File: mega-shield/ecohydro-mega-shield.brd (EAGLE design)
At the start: 101.6 x 92.7 mm, 99 parts, among them IC1 MCP1700-330, IC2 DS1306E, IC3 74HC125D, IC4 AP3211KTR, Q1 IRLM5103, Q10 PBSS4021NT,215, Q11 PBSS4021NT,215, Q12 PBSS4021NT,215, Q13 PBSS4021NT,215, Q14 PBSS4021NT,215, Q15 PBSS4021NT,215, Q16 PBSS4021NT,215, Q17 IRLM5103, Q18 IRLM5103, Q19 IRLM5103, Q2 IRLM5103, Q20 PBSS4021NT,215, Q21 PBSS4021NT,215, Q22 PBSS4021NT,215, Q3 IRLM5103, Q4 IRLM5103, Q5 IRLM5103, Q6 IRLM5103, Q7 IRLM5103, Q8 IRLM5103, Q9 PBSS4021NT,215, U1 ARDUINO-MEGA

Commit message: Rev 1.1 with some fixes, not sent for production yet
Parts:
- removed A7: MKDS1/3-3,81, con-phoenix-381:3POL381
- added A15: MKDS1/3-3,81, con-phoenix-381:3POL381
- Q10, Q11, Q12, Q13, Q14, Q15, Q16, Q20, Q21, Q22, Q9: device semiconductors:SOT-23 -> semiconductors:SOT23
- R19: value 470R -> 1k; device passives:R0603-N -> passives:R0805
- moved A14 16.5 mm to (88.9, 4.45), turned to 0 degrees
- moved A12 14.0 mm to (61.0, 4.45)
- moved A9 14.0 mm to (19.1, 4.45)
- moved A8 14.0 mm to (5.08, 4.45)
- moved A10 14.0 mm to (33.0, 4.45)
- moved A11 14.0 mm to (47.0, 4.45)
- moved A13 14.0 mm to (74.9, 4.45)
- moved Q22 2.55 mm to (48.2, 71.0)
- moved Q20 1.58 mm to (12.3, 71.0)
- moved Q21 1.58 mm to (29.4, 71.0)
- moved Q17 1.00 mm to (51.8, 73.7)
- moved R20 1.00 mm to (51.8, 70.5)
- moved Q18 0.50 mm to (33.5, 73.7)
- moved Q19 0.50 mm to (15.7, 73.7)
- moved Q9 0.50 mm to (82.4, 23.5)
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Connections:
- removed net N$5 (its old number): A7.2, U1.A7
- new net N$76: U1.3
- new net N$77: U1.2
- new net N$88: A15.2, U1.A15
- net GND: now also A15.3; no longer A7.3
- net N$10: now also A14.1; no longer A13.1
- net N$11: now also A13.1; no longer A12.1
- net N$12: now also A12.1; no longer A11.1
- net N$13: now also A11.1; no longer A10.1
- net N$14: now also U1.20; no longer U1.5
- net N$4: now also A8.1; no longer A7.1
- net N$6: now also A9.1; no longer A8.1
- net N$73: no longer U1.3
- net N$75: no longer U1.4
- net N$8: now also A10.1; no longer A9.1
- net N$9: now also A15.1; no longer A14.1
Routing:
- net N$5 (its old number): track 45.4 -> 0.00 mm
- net N$88: track 0.00 -> 38.0 mm
- net N$30: track 45.7 -> 30.3 mm
- net N$20: track 34.5 -> 19.9 mm
- net N$7: track 27.3 -> 41.6 mm
- net N$17: track 17.2 -> 30.1 mm
- net N$5: track 39.0 -> 50.5 mm
- net N$73: track 16.1 -> 9.40 mm
- net N$18: track 23.9 -> 18.3 mm
- net N$14: track 56.9 -> 53.8 mm
- net N$75: track 14.1 -> 11.5 mm
- net N$70: track 4.46 -> 5.94 mm
- net N$34: track 4.20 -> 3.06 mm
- net FETG8: track 4.78 -> 5.73 mm
- net FETG7: track 4.78 -> 5.73 mm
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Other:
- board text added: "+ 15 G"
- board text added: "1A"
- board text added: "4A"
- board text added: "v1.1 January 2015"
- board text removed: "+ 7 G"
- board text removed: "v1.0 December 2014"

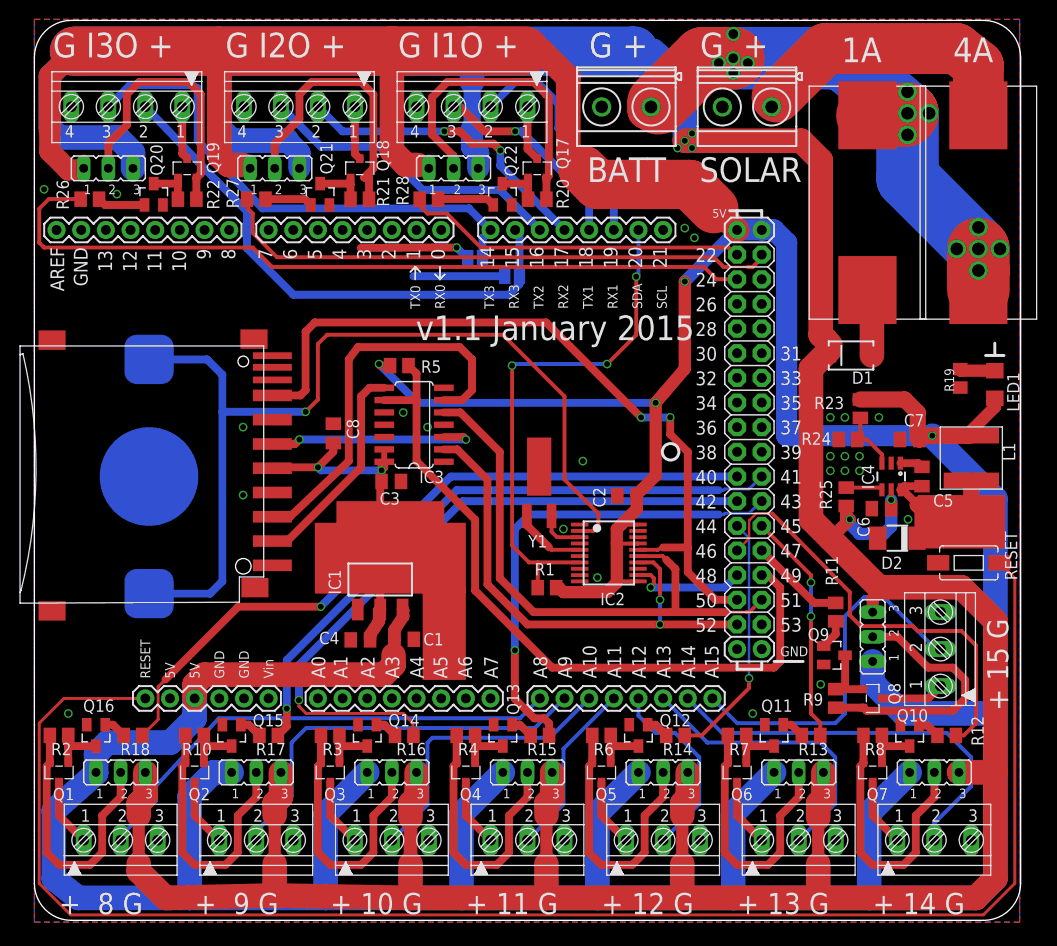
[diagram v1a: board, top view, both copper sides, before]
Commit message: Rev 1.2 Fixes - Change R19 to 4k7 - GSM shield bypass pins are out by 1 (should be 2 & 3, not 3 & 4) - Change pads on Batt and Solar connectors - Change package on xtal
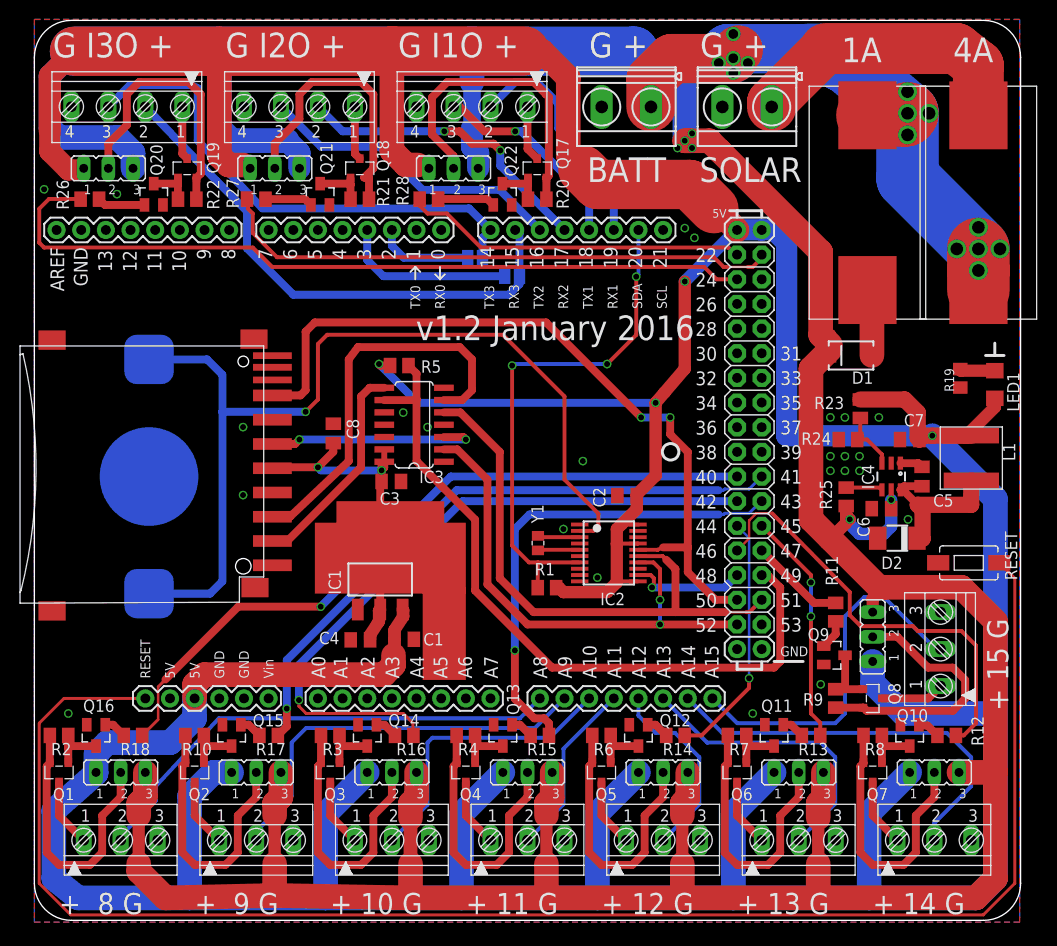
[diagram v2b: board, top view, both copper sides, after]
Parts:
- BATT, SOLAR: device con-phoenix-508:MKDSN1,5/2-5,08 -> mechanical:MKDSN1,5/2-5,08
- R19: value 1k -> 4k7
- Y1: value (none) -> 32.768KHZ; device SparkFun-FreqCtrl:CRYSTAL-32KHZ-SMD -> Seeed-Crystal Oscillator-2016:X2-SMD-L2.0X1.2X0.55MM
- moved Y1 2.80 mm to (51.9, 35.1), turned to 90 degrees
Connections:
- removed net N$75: SJ1.1
- removed net N$76: U1.3
- net N$1: now also IC2.5, Y1.1; no longer IC2.3, Y1.X2
- net N$3: now also IC2.3, Y1.2; no longer IC2.5, Y1.X1
- net N$73: now also U1.3
- net N$77: now also SJ1.1
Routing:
- net N$75: track 11.5 -> 0.00 mm, vias 1 -> 0
- net N$77: track 0.00 -> 9.95 mm
- net N$73: track 9.40 -> 17.9 mm
- net +12V: track 417.9 -> 412.9 mm
- net N$44: track 78.6 -> 82.6 mm
- net N$3: track 7.45 -> 4.36 mm
- net N$45: track 30.4 -> 29.8 mm
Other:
- board text added: "v1.2 January 2016"
- board text removed: "v1.1 January 2015"

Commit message: Rev 1.4 - Reduced board size by 2mm to fit 10x10 economy pcb mfg
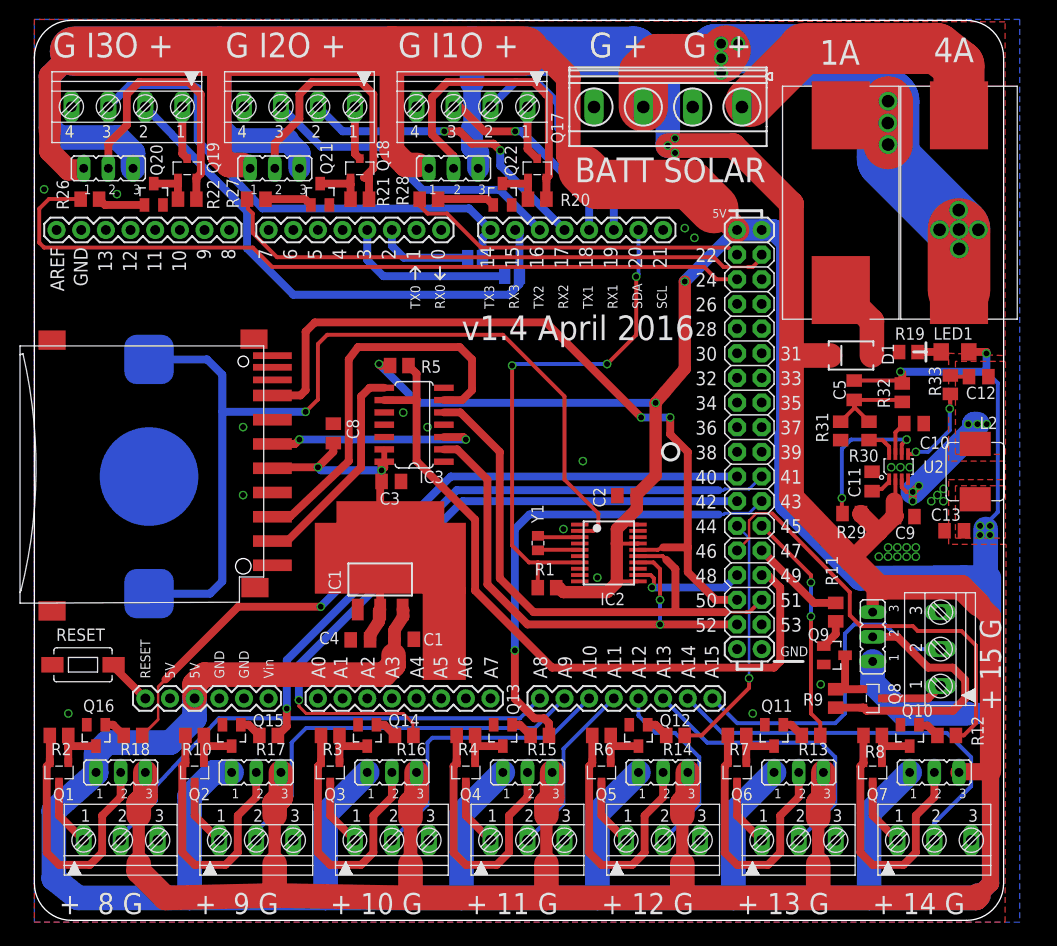
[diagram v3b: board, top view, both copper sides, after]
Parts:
- removed BATT, SOLAR: MKDSN1,5/2-5,08, mechanical:MKDSN1,5/2-5,08
- removed C6: 10uF/25V, rcl:C0805K
- removed C7: 22uF/6.3V, rcl:C0805K
- removed D2: BD240A, semiconductors:DO-214AC
- removed IC4: AP3211KTR, semiconductors:SOT23-6
- removed L1: 10uH, passives:L6028
- removed R23: 49K9, rcl:M0805
- removed R24: 9K53, rcl:M0805
- removed R25: 10K, rcl:M0805
- added C10, C12: 0.1uF, rcl:C0805K
- added C11: 22nF, rcl:C0805K
- added C13: 47uF/10V, rcl:C0805K
- added C9: 22uF/25V, rcl:C0805K
- added L2: 10UH, Seeed-Inductor-2016:SMD-2P-L6.0XW6.0XH3.0MM
- added R29: 100K, rcl:M0805
- added R30: 49K9, rcl:M0805
- added R31: 7K68, rcl:M0805
- added R32: 40K2, rcl:M0805
- added R33: 10R, rcl:M0805
- added U2: MP1496DJ-SOT23-8, Seeed-IC-2016:SOT-23-8
- added X1: MKDSN1,5/4-5,08, mechanical:MKDSN1,5/4-5,08
- C5: value 10nF -> 22nF
- moved RESET 91.9 mm to (5.01, 22.5)
- moved C5 11.3 mm to (84.5, 50.8), turned to 90 degrees
- moved R19 6.00 mm to (90.0, 54.7), turned to 0 degrees
- moved LED1 5.30 mm to (94.8, 54.7), turned to 0 degrees
- moved FS1 2.75 mm to (83.1, 70.1)
- moved FS2 2.00 mm to (95.2, 70.1)
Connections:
- removed net N$62: C5.1, IC4.1
- removed net N$63: C5.2, D2.C, IC4.6, L1.1
- removed net N$64: IC4.4, R25.1
- removed net N$66: IC4.3, R23.2, R24.1
- new net N$72: C10.1, U2.7
- new net N$74: R29.1, U2.6
- new net N$75: C11.1, U2.1
- new net N$78: R30.2, U2.8
- new net N$79: C5.1, R30.1, R31.1, R32.1
- new net N$80: C12.2, L2.1, U2.3
- new net N$82: R33.2, U2.5
- new net N$83: C12.1, R33.1
- net +12V: now also C9.1, R29.2, U2.2; no longer C6.1, IC4.5, R25.2
- net +5V: now also C13.1, C5.2, L2.2, R32.2; no longer C7.1, L1.2, R23.1
- net GND: now also C10.2, C11.2, C13.2, C9.2, R31.2, U2.4, X1.2, X1.4; no longer BATT.2, C6.2, C7.2, D2.A, IC4.2, R24.2, SOLAR.2
- net N$44: now also X1.3; no longer BATT.1
- net N$45: now also X1.1; no longer SOLAR.1
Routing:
- net N$2: track 165.4 -> 4.83 mm
- net +5V: track 581.5 -> 601.3 mm, vias 4 -> 9
- net N$63: track 17.1 -> 0.00 mm
- net N$74: track 0.00 -> 15.5 mm, vias 0 -> 2
- net N$80: track 0.00 -> 13.9 mm, vias 0 -> 6
- net N$79: track 0.00 -> 10.7 mm
- net N$82: track 0.00 -> 9.08 mm, vias 0 -> 2
- net N$66: track 6.44 -> 0.00 mm
- net N$64: track 3.78 -> 0.00 mm
- net N$72: track 0.00 -> 3.52 mm
- net N$78: track 0.00 -> 3.11 mm
- net N$88: track 38.0 -> 35.1 mm
- net N$75: track 0.00 -> 2.41 mm
- net N$62: track 2.38 -> 0.00 mm
- net N$44: track 82.6 -> 84.7 mm, vias 14 -> 12
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- added copper zone on layer 1, net +5V
- added copper zone on layer 1, net N$80
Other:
- board size 101.6 x 92.7 mm -> 99.8 x 92.7 mm
- board text added: "BATT SOLAR"
- board text added: "UBCEcoHydro Arduino Mega Shield"
- board text added: "v1.4 April 2016"
- board text removed: "v1.2 January 2016"

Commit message: Rev 1.5 - Add fiducials
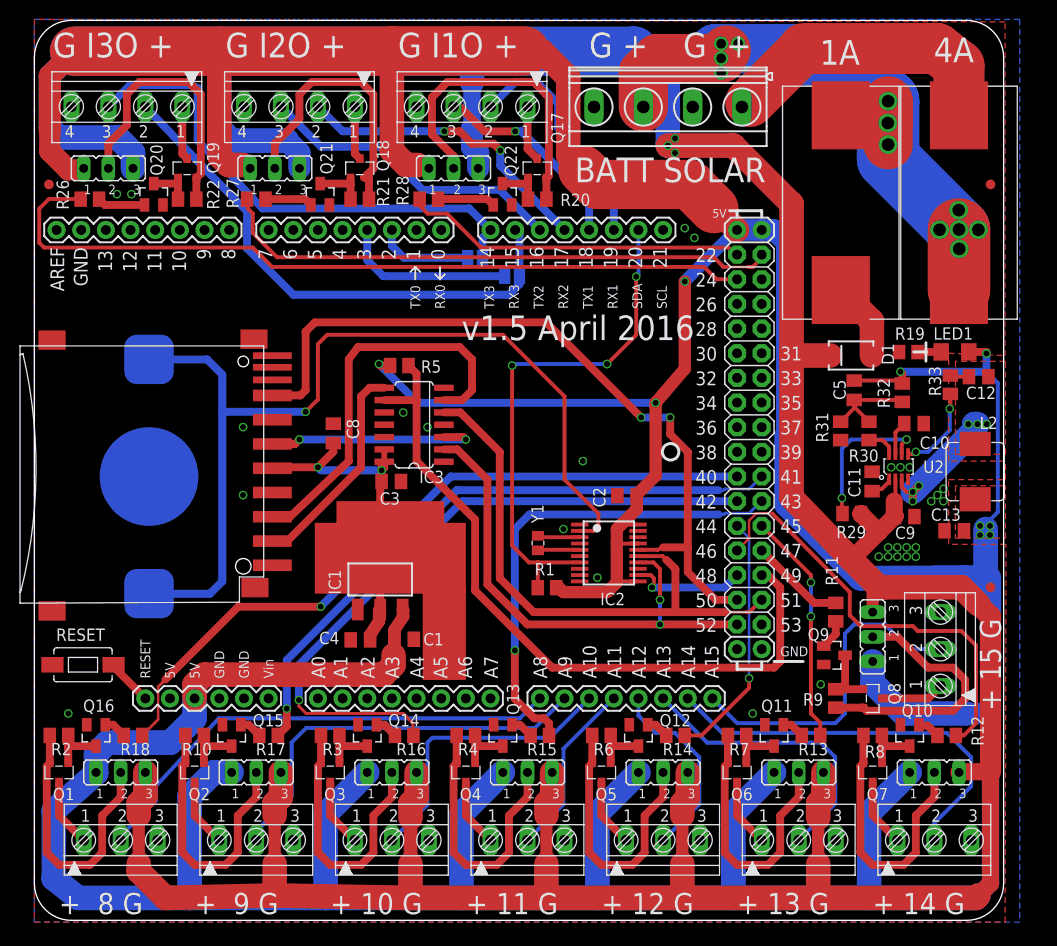
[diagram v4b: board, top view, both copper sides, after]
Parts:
- added U$2, U$3, U$4: FIDUCIAL, adafruit:FIDUCIAL_1MM
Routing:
- net N$44: track 84.7 -> 86.7 mm
- net +12V: track 410.8 -> 412.3 mm
- net +5V: track 601.3 -> 602.4 mm
- net N$45: track 29.6 -> 30.6 mm
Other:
- board text added: "v1.5 April 2016"
- board text removed: "v1.4 April 2016"

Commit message: Fix designators on power select jumpers
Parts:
- removed JP-A7: (no value), jumper:JP2
- added JP-A15: (no value), jumper:JP2
- moved JP-A14 15.3 mm to (92.7, 11.4), turned to 0 degrees
- moved JP-A10 14.0 mm to (36.8, 11.4)
- moved JP-A11 14.0 mm to (50.8, 11.4)
- moved JP-A12 14.0 mm to (64.8, 11.4)
- moved JP-A13 14.0 mm to (78.7, 11.4)
- moved JP-A8 14.0 mm to (8.89, 11.4)
- moved JP-A9 14.0 mm to (22.9, 11.4)
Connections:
- net +12V: now also JP-A15.3; no longer JP-A7.3
- net +5V: now also JP-A15.1; no longer JP-A7.1
- net N$16: now also JP-A8.2; no longer JP-A7.2
- net N$19: now also JP-A10.2; no longer JP-A9.2
- net N$21: now also JP-A15.2; no longer JP-A14.2
- net N$22: now also JP-A14.2; no longer JP-A13.2
- net N$23: now also JP-A13.2; no longer JP-A12.2
- net N$24: now also JP-A12.2; no longer JP-A11.2
- net N$25: now also JP-A11.2; no longer JP-A10.2
- net N$26: now also JP-A9.2; no longer JP-A8.2
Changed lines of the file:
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@@
 <attribute name="VALUE" x="98.425" y="18.415" size="1.27" layer="27" rot="R90"/>
 </element>
-<element name="JP-A7" library="jumper" package="JP2" value="" x="8.89" y="11.43" smashed="yes">
+<element name="JP-A8" library="jumper" package="JP2" value="" x="8.89" y="11.43" smashed="yes">
 <attribute name="VALUE" x="5.334" y="7.112" size="1.27" layer="27" ratio="10"/>
 </element>
-<element name="JP-A8" library="jumper" package="JP2" value="" x="22.86" y="11.43" smashed="yes">
+<element name="JP-A9" library="jumper" package="JP2" value="" x="22.86" y="11.43" smashed="yes">
 <attribute name="VALUE" x="19.304" y="7.112" size="1.27" layer="27" ratio="10"/>
 </element>
-<element name="JP-A9" library="jumper" package="JP2" value="" x="36.83" y="11.43" smashed="yes">
+<element name="JP-A10" library="jumper" package="JP2" value="" x="36.83" y="11.43" smashed="yes">
 <attribute name="VALUE" x="33.274" y="7.112" size="1.27" layer="27" ratio="10"/>
 </element>
-<element name="JP-A10" library="jumper" package="JP2" value="" x="50.8" y="11.43" smashed="yes">
+<element name="JP-A11" library="jumper" package="JP2" value="" x="50.8" y="11.43" smashed="yes">
 <attribute name="VALUE" x="47.244" y="7.112" size="1.27" layer="27" ratio="10"/>
 </element>
-<element name="JP-A11" library="jumper" package="JP2" value="" x="64.77" y="11.43" smashed="yes">
+<element name="JP-A12" library="jumper" package="JP2" value="" x="64.77" y="11.43" smashed="yes">
 <attribute name="VALUE" x="61.214" y="7.112" size="1.27" layer="27" ratio="10"/>
 </element>
-<element name="JP-A12" library="jumper" package="JP2" value="" x="78.74" y="11.43" smashed="yes">
+<element name="JP-A13" library="jumper" package="JP2" value="" x="78.74" y="11.43" smashed="yes">
 <attribute name="VALUE" x="75.184" y="7.112" size="1.27" layer="27" ratio="10"/>
 </element>
-<element name="JP-A13" library="jumper" package="JP2" value="" x="92.71" y="11.43" smashed="yes">
+<element name="JP-A14" library="jumper" package="JP2" value="" x="92.71" y="11.43" smashed="yes">
 <attribute name="VALUE" x="89.154" y="7.112" size="1.27" layer="27" ratio="10"/>
 </element>
-<element name="JP-A14" library="jumper" package="JP2" value="" x="86.36" y="25.4" smashed="yes" rot="R90">
+<element name="JP-A15" library="jumper" package="JP2" value="" x="86.36" y="25.4" smashed="yes" rot="R90">
 <attribute name="VALUE" x="90.678" y="21.844" size="1.27" layer="27" ratio="10" rot="R90"/>
 </element>
@@
 <contactref element="IC2" pad="17"/>
 <contactref element="R1" pad="2"/>
-<contactref element="JP-A14" pad="1"/>
-<contactref element="JP-A7" pad="1"/>
+<contactref element="JP-A15" pad="1"/>
 <contactref element="JP-A8" pad="1"/>
 <contactref element="JP-A9" pad="1"/>
@@
 <contactref element="JP-A12" pad="1"/>
 <contactref element="JP-A13" pad="1"/>
+<contactref element="JP-A14" pad="1"/>
 <contactref element="LED1" pad="A"/>
 <contactref element="JP-S2" pad="1"/>
@@
 </signal>
 <signal name="+12V">
+<contactref element="JP-A15" pad="3"/>
 <contactref element="JP-A14" pad="3"/>
 <contactref element="JP-A13" pad="3"/>
@@
 <contactref element="JP-A9" pad="3"/>
 <contactref element="JP-A8" pad="3"/>
-<contactref element="JP-A7" pad="3"/>
 <contactref element="D1" pad="C"/>
 <contactref element="JP-S1" pad="3"/>
@@
 <signal name="N$16">
 <contactref element="Q1" pad="2"/>
-<contactref element="JP-A7" pad="2"/>
+<contactref element="JP-A8" pad="2"/>
 <contactref element="R2" pad="2"/>
 <wire x1="1.59" y1="12.43" x2="1.59" y2="15.24" width="0.8128" layer="1"/>
@@
 <signal name="N$19">
 <contactref element="Q3" pad="2"/>
-<contactref element="JP-A9" pad="2"/>
+<contactref element="JP-A10" pad="2"/>
 <contactref element="R3" pad="2"/>
 <wire x1="29.53" y1="12.43" x2="29.53" y2="15.24" width="0.8128" layer="1"/>
@@
 </signal>
 <signal name="N$21">
-<contactref element="JP-A14" pad="2"/>
+<contactref element="JP-A15" pad="2"/>
 <contactref element="Q8" pad="2"/>
 <contactref element="R9" pad="2"/>
@@
 </signal>
 <signal name="N$22">
-<contactref element="JP-A13" pad="2"/>
+<contactref element="JP-A14" pad="2"/>
 <contactref element="Q7" pad="2"/>
 <contactref element="R8" pad="2"/>
@@
 <signal name="N$23">
 <contactref element="Q6" pad="2"/>
-<contactref element="JP-A12" pad="2"/>
+<contactref element="JP-A13" pad="2"/>
 <contactref element="R7" pad="2"/>
 <wire x1="71.44" y1="12.43" x2="71.44" y2="15.24" width="0.8128" layer="1"/>
@@
 <signal name="N$24">
 <contactref element="Q5" pad="2"/>
-<contactref element="JP-A11" pad="2"/>
+<contactref element="JP-A12" pad="2"/>
 <contactref element="R6" pad="2"/>
 <wire x1="57.47" y1="12.43" x2="57.47" y2="15.24" width="0.8128" layer="1"/>
@@
 <signal name="N$25">
 <contactref element="Q4" pad="2"/>
-<contactref element="JP-A10" pad="2"/>
+<contactref element="JP-A11" pad="2"/>
 <contactref element="R4" pad="2"/>
 <wire x1="43.5" y1="12.43" x2="43.5" y2="15.24" width="0.8128" layer="1"/>
@@
 <signal name="N$26">
 <contactref element="Q2" pad="2"/>
-<contactref element="JP-A8" pad="2"/>
+<contactref element="JP-A9" pad="2"/>
 <contactref element="R10" pad="2"/>
 <wire x1="15.56" y1="15.24" x2="15.56" y2="12.43" width="0.8128" layer="1"/>
